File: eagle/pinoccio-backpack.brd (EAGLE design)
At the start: 25.4 x 43.2 mm, 5 parts, among them J1 AVR_SPI_PRG_6

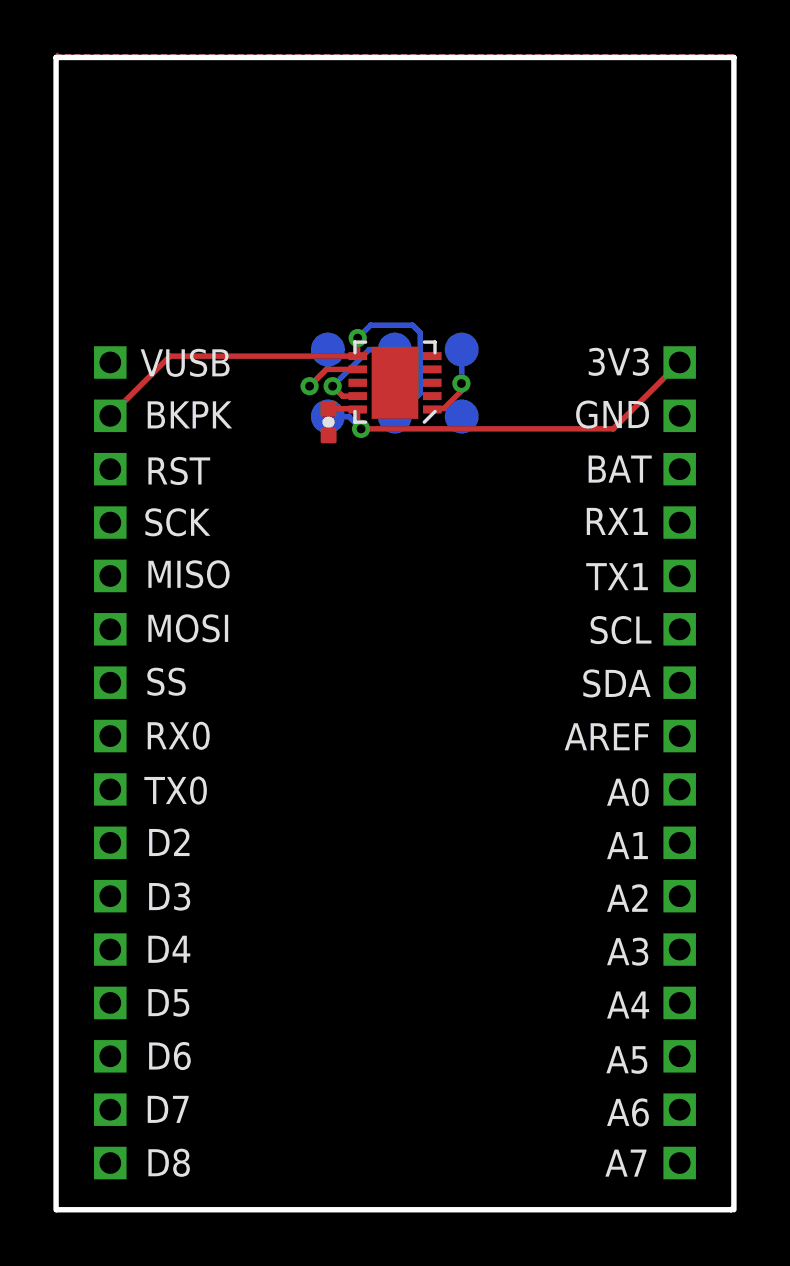
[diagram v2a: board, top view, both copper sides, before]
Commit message: Updated to v0.13 layout to match latest header location changes
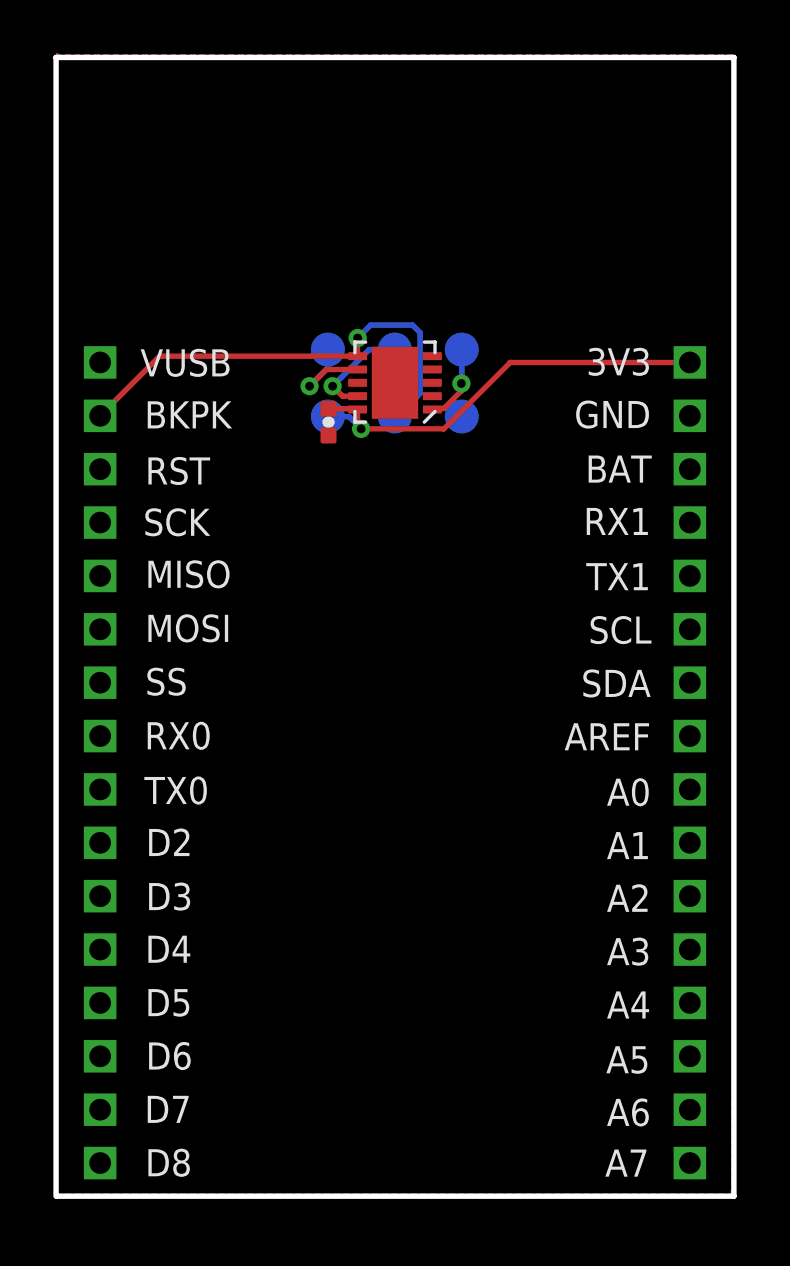
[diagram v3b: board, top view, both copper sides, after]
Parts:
- moved JP-R 0.38 mm to (23.7, 39.4)
- moved JP-L 0.38 mm to (1.65, 39.4)
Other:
- board size 25.4 x 43.2 mm -> 25.4 x 42.7 mm
- board text added: "Pinoccio(tm) Backpack Reference v0.13"
- board text added: "tiny13A"
- board text removed: "Pinoccio(tm) Backpack Reference v0.11"
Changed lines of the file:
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@@
 <board>
 <plain>
-<wire x1="0" y1="7.62" x2="0" y2="50.8" width="0.2032" layer="20"/>
+<wire x1="0" y1="8.128" x2="0" y2="50.8" width="0.2032" layer="20"/>
 <text x="3.2604" y="32.873" size="1.016" layer="21" font="vector" ratio="15">SCK</text>
 <text x="3.3366" y="30.9238" size="1.016" layer="21" font="vector" ratio="15">MISO</text>
@@
 <text x="22.3174" y="29.8508" size="1.016" layer="21" font="vector" ratio="15" rot="R180">SCL</text>
 <text x="-10.414" y="-6.604" size="1.27" layer="51" font="vector" ratio="15">Design by: Eric Jennings for Pinoccio</text>
-<text x="-10.3632" y="-4.8514" size="1.778" layer="51" font="vector" ratio="15">Pinoccio(tm) Backpack Reference v0.11</text>
+<text x="-10.3632" y="-4.8514" size="1.778" layer="51" font="vector" ratio="15">Pinoccio(tm) Backpack Reference v0.13</text>
 <wire x1="0" y1="50.8" x2="25.4" y2="50.8" width="0.2032" layer="20"/>
 <text x="3.3366" y="28.8984" size="1.016" layer="21" font="vector" ratio="15">MOSI</text>
@@
 <text x="22.292" y="25.8508" size="1.016" layer="21" font="vector" ratio="15" rot="R180">AREF</text>
 <text x="-10.4648" y="-10.2362" size="1.27" layer="51" font="vector" ratio="15">Licensed under Creative Commons Attribution 3.0 Unported.</text>
-<wire x1="25.4" y1="7.62" x2="25.4" y2="50.8" width="0.2032" layer="20"/>
-<wire x1="0.0254" y1="7.62" x2="25.2984" y2="7.62" width="0.2032" layer="20"/>
-<wire x1="25.2984" y1="7.62" x2="25.3238" y2="7.6454" width="0.2032" layer="20"/>
+<wire x1="25.4" y1="8.128" x2="25.4" y2="50.8" width="0.2032" layer="20"/>
+<wire x1="0.0254" y1="8.128" x2="25.4" y2="8.128" width="0.2032" layer="20"/>
+<text x="14.986" y="41.4528" size="0.8128" layer="22" ratio="15" rot="MR0">tiny13A</text>
 </plain>
 <attributes>
@@
 </autorouter>
 <elements>
-<element name="JP-R" library="Pinoccio" package="1X16_2MM" value="M162MM" x="23.368" y="39.37" locked="yes" smashed="yes" rot="R270"/>
-<element name="JP-L" library="Pinoccio" package="1X16_2MM" value="M162MM" x="2.032" y="39.37" locked="yes" smashed="yes" rot="R270"/>
+<element name="JP-R" library="Pinoccio" package="1X16_2MM" value="M162MM" x="23.749" y="39.37" locked="yes" smashed="yes" rot="R270"/>
+<element name="JP-L" library="Pinoccio" package="1X16_2MM" value="M162MM" x="1.651" y="39.37" locked="yes" smashed="yes" rot="R270"/>
 <element name="U$3" library="Pinoccio" package="QFN-10" value="ATTINY13QFN10" x="12.7" y="38.608" rot="R180"/>
-<element name="J1" library="Pinoccio" package="2X3-PAD" value="AVR_SPI_PRG_6" x="10.1854" y="39.8526" rot="MR180"/>
+<element name="J1" library="Pinoccio" package="2X3-PAD" value="AVR_SPI_PRG_6" x="10.1854" y="39.8526" locked="yes" rot="MR180"/>
 <element name="C7" library="Pinoccio" package="0402-CAP" value="0.1uf" x="10.2108" y="37.1348" smashed="yes" rot="R270"/>
 </elements>
@@
 <vertex x="0.0762" y="50.9524"/>
 <vertex x="0.0254" y="50.9524"/>
-<vertex x="0.0254" y="7.5946"/>
-<vertex x="25.3746" y="7.5946"/>
-<vertex x="25.3746" y="7.62"/>
+<vertex x="-0.0254" y="8.2042"/>
+<vertex x="25.3238" y="8.2042"/>
+<vertex x="25.3492" y="8.2296"/>
 <vertex x="25.3746" y="50.9016"/>
 <vertex x="0.0762" y="50.9016"/>
@@
 <vertex x="0.0762" y="50.7746"/>
 <vertex x="0.0254" y="50.7746"/>
-<vertex x="0.0254" y="7.6454"/>
-<vertex x="24.892" y="7.62"/>
-<vertex x="25.0698" y="7.62"/>
-<vertex x="25.3746" y="7.5946"/>
+<vertex x="-0.0254" y="8.2042"/>
+<vertex x="24.8412" y="8.1788"/>
+<vertex x="25.2984" y="8.1788"/>
+<vertex x="25.3238" y="8.636"/>
 <vertex x="25.3746" y="50.8762"/>
 <vertex x="0.1016" y="50.8762"/>
@@
 <signal name="MOSI">
 <contactref element="JP-L" pad="P$6"/>
-<wire x1="2.032" y1="29.337" x2="2.032" y2="29.37" width="0.3048" layer="16"/>
 </signal>
 <signal name="SCK">
 <contactref element="JP-L" pad="P$4"/>
-<wire x1="2.032" y1="33.3756" x2="2.032" y2="33.37" width="0.3048" layer="16"/>
 </signal>
 <signal name="MISO">
 <contactref element="JP-L" pad="P$5"/>
-<wire x1="2.032" y1="31.369" x2="2.032" y2="31.37" width="0.3048" layer="16"/>
 </signal>
 <signal name="RX1">
 <contactref element="JP-R" pad="P$4"/>
-<wire x1="23.368" y1="33.3502" x2="23.368" y2="33.37" width="0.3048" layer="16"/>
 </signal>
 <signal name="TX1">
 <contactref element="JP-R" pad="P$5"/>
-<wire x1="23.368" y1="31.3436" x2="23.368" y2="31.37" width="0.3048" layer="16"/>
 </signal>
 <signal name="AREF">
 <contactref element="JP-R" pad="P$8"/>
-<wire x1="23.368" y1="25.3492" x2="23.368" y2="25.37" width="0.3048" layer="16"/>
 </signal>
 <signal name="VUSB">
@@
 <signal name="SSN">
 <contactref element="JP-L" pad="P$7"/>
-<wire x1="2.032" y1="27.3558" x2="2.032" y2="27.37" width="0.3048" layer="16"/>
 </signal>
 <signal name="SCL">
 <contactref element="JP-R" pad="P$6"/>
-<wire x1="23.368" y1="29.3624" x2="23.368" y2="29.37" width="0.3048" layer="16"/>
 </signal>
 <signal name="SDA">
 <contactref element="JP-R" pad="P$7"/>
-<wire x1="23.368" y1="27.3812" x2="23.368" y2="27.37" width="0.3048" layer="16"/>
 </signal>
 <signal name="RX0">
 <contactref element="JP-L" pad="P$8"/>
-<wire x1="2.032" y1="25.3492" x2="2.032" y2="25.37" width="0.3048" layer="16"/>
 </signal>
 <signal name="TX0">
 <contactref element="JP-L" pad="P$9"/>
-<wire x1="2.032" y1="23.368" x2="2.032" y2="23.37" width="0.3048" layer="16"/>
 </signal>
 <signal name="RESET">
 <contactref element="JP-L" pad="P$3"/>
-<wire x1="2.032" y1="35.3568" x2="2.032" y2="35.37" width="0.3048" layer="16"/>
 </signal>
 <signal name="A0">
 <contactref element="JP-R" pad="P$9"/>
-<wire x1="23.368" y1="23.368" x2="23.368" y2="23.37" width="0.3048" layer="16"/>
 </signal>
 <signal name="A1">
 <contactref element="JP-R" pad="P$10"/>
-<wire x1="23.368" y1="21.3614" x2="23.368" y2="21.37" width="0.3048" layer="16"/>
 </signal>
 <signal name="A2">
 <contactref element="JP-R" pad="P$11"/>
-<wire x1="23.368" y1="19.3802" x2="23.368" y2="19.37" width="0.3048" layer="16"/>
 </signal>
 <signal name="A3">
 <contactref element="JP-R" pad="P$12"/>
-<wire x1="23.368" y1="17.3736" x2="23.368" y2="17.37" width="0.3048" layer="16"/>
 </signal>
 <signal name="A4">
 <contactref element="JP-R" pad="P$13"/>
-<wire x1="23.368" y1="15.367" x2="23.368" y2="15.37" width="0.3048" layer="16"/>
 </signal>
 <signal name="A5">
 <contactref element="JP-R" pad="P$14"/>
-<wire x1="23.368" y1="13.3858" x2="23.368" y2="13.37" width="0.3048" layer="16"/>
 </signal>
 <signal name="A6">
 <contactref element="JP-R" pad="P$15"/>
-<wire x1="23.368" y1="11.3792" x2="23.368" y2="11.37" width="0.3048" layer="16"/>
 </signal>
 <signal name="A7">
 <contactref element="JP-R" pad="P$16"/>
-<wire x1="23.368" y1="9.3726" x2="23.368" y2="9.37" width="0.3048" layer="16"/>
 </signal>
 <signal name="VCC-AE">
@@
 <wire x1="11.276" y1="37.584" x2="11.2252" y2="37.6348" width="0.2032" layer="1"/>
 <wire x1="11.2252" y1="37.6348" x2="10.2108" y2="37.6348" width="0.2032" layer="1"/>
-<wire x1="23.368" y1="39.37" x2="20.8788" y2="36.8808" width="0.2032" layer="1"/>
-<wire x1="20.8788" y1="36.8808" x2="11.43" y2="36.8808" width="0.2032" layer="1"/>
+<wire x1="23.749" y1="39.37" x2="17.018" y2="39.37" width="0.2032" layer="1"/>
+<wire x1="17.018" y1="39.37" x2="14.5288" y2="36.8808" width="0.2032" layer="1"/>
+<wire x1="14.5288" y1="36.8808" x2="11.43" y2="36.8808" width="0.2032" layer="1"/>
 </signal>
 <signal name="VIN">
@@
 <signal name="D2">
 <contactref element="JP-L" pad="P$10"/>
-<wire x1="2.032" y1="21.3614" x2="2.032" y2="21.37" width="0.3048" layer="16"/>
 </signal>
 <signal name="D3">
 <contactref element="JP-L" pad="P$11"/>
-<wire x1="2.032" y1="19.3802" x2="2.032" y2="19.37" width="0.3048" layer="16"/>
 </signal>
 <signal name="D4">
 <contactref element="JP-L" pad="P$12"/>
-<wire x1="2.032" y1="17.3736" x2="2.032" y2="17.37" width="0.3048" layer="16"/>
 </signal>
 <signal name="D5">
 <contactref element="JP-L" pad="P$13"/>
-<wire x1="2.032" y1="15.367" x2="2.032" y2="15.37" width="0.3048" layer="16"/>
 </signal>
 <signal name="D6">
 <contactref element="JP-L" pad="P$14"/>
-<wire x1="2.032" y1="13.3604" x2="2.032" y2="13.37" width="0.3048" layer="16"/>
 </signal>
 <signal name="D7">
 <contactref element="JP-L" pad="P$15"/>
-<wire x1="2.032" y1="11.4046" x2="2.032" y2="11.37" width="0.3048" layer="16"/>
 </signal>
 <signal name="D8">
 <contactref element="JP-L" pad="P$16"/>
-<wire x1="2.032" y1="9.3726" x2="2.032" y2="9.37" width="0.3048" layer="16"/>
 </signal>
 <signal name="BKPK-BUS">
@@
 <wire x1="11.303" y1="40.2844" x2="11.3" y2="40.2814" width="0.2032" layer="1"/>
 <wire x1="11.3" y1="40.2814" x2="11.3" y2="39.608" width="0.2032" layer="1"/>
-<wire x1="2.032" y1="37.37" x2="4.27" y2="39.608" width="0.2032" layer="1"/>
-<wire x1="4.27" y1="39.608" x2="11.3" y2="39.608" width="0.2032" layer="1"/>
+<wire x1="1.651" y1="37.37" x2="3.889" y2="39.608" width="0.2032" layer="1"/>
+<wire x1="3.889" y1="39.608" x2="11.3" y2="39.608" width="0.2032" layer="1"/>
 </signal>
 <signal name="VBAT">
